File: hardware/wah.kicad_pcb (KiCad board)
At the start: 4 copper layers, 99.1 x 54.5 mm, 32 parts, among them J1 Barrel_Jack_Switch, J2 In, J3 Out, SW1 SW_Push_3PDT, U1 TL072, U2 L78L05_TO92

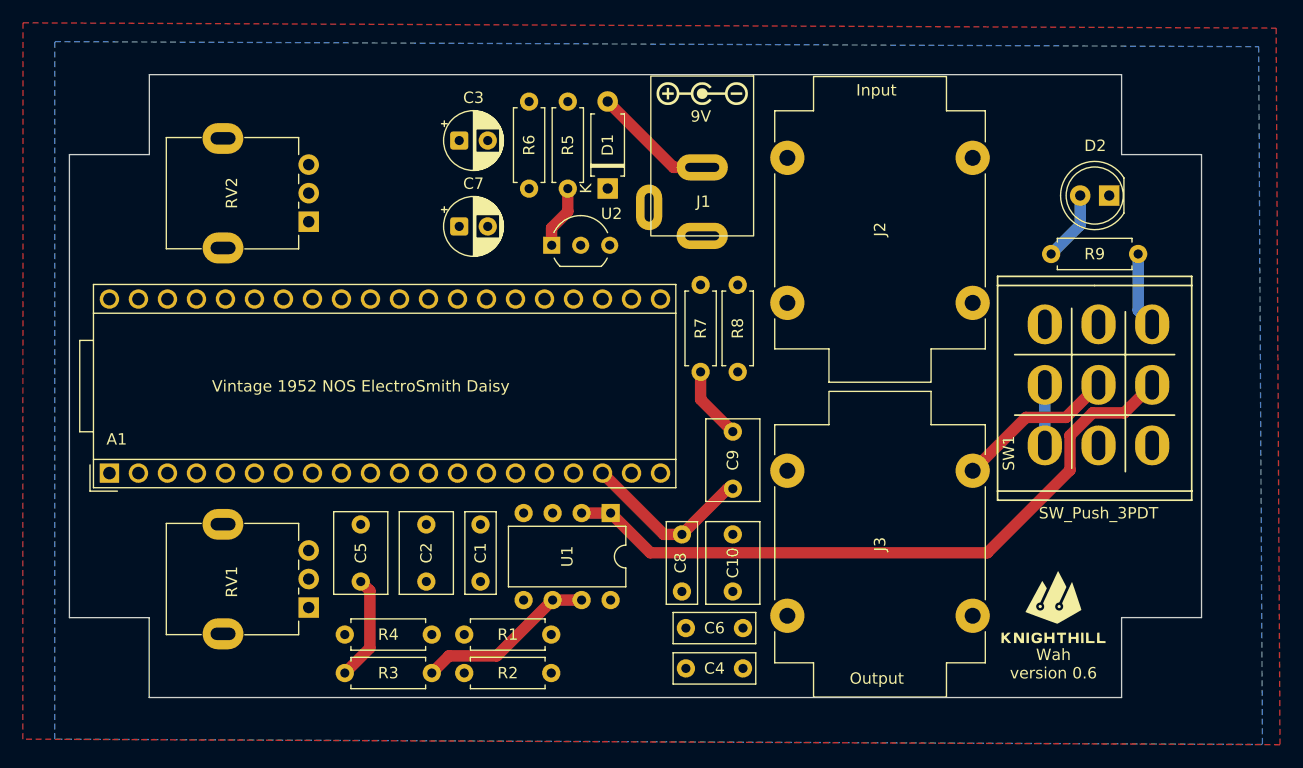
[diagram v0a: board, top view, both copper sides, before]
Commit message: move opamp under daisy
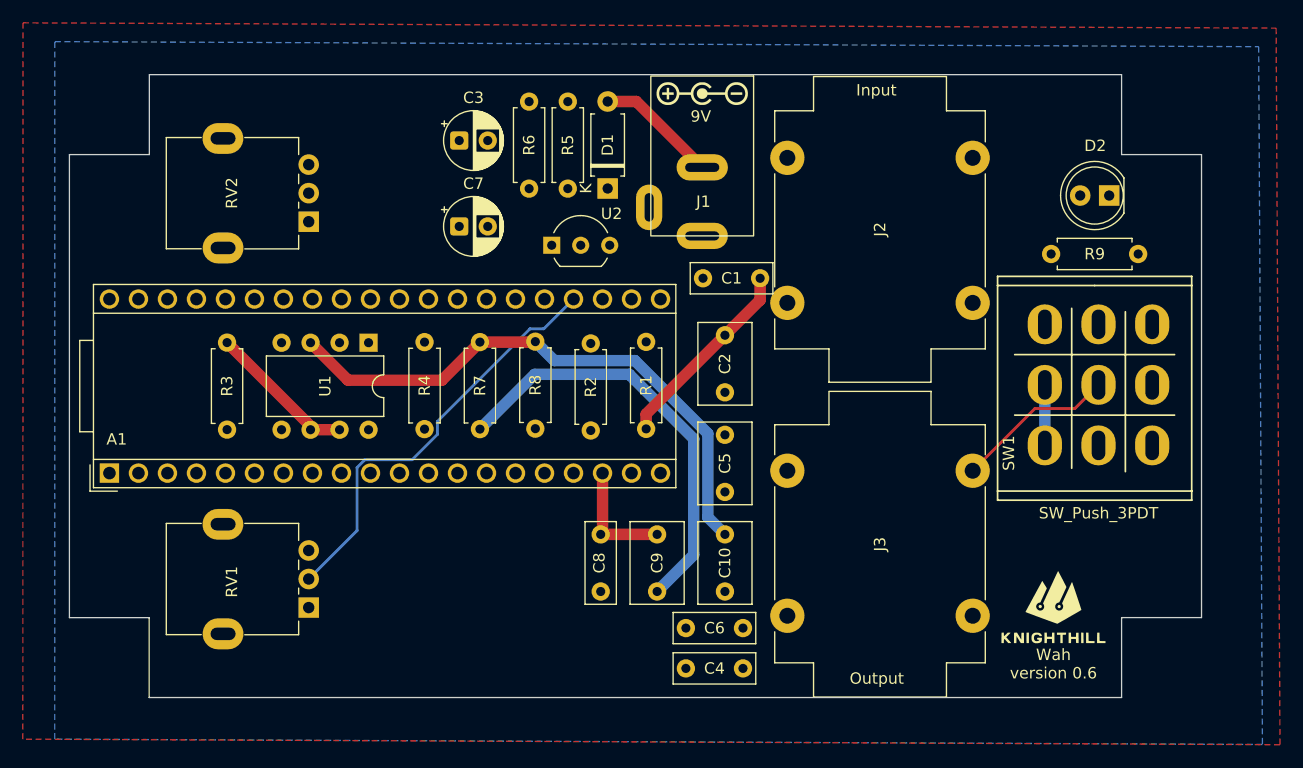
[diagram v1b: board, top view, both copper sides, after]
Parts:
- moved C1 36.1 mm to (102.9, 51.0), turned to 180 degrees
- moved R3 34.0 mm to (56.2, 56.6), turned to -90 degrees
- moved C5 32.8 mm to (99.8, 69.7)
- moved C2 31.0 mm to (99.8, 56.0)
- moved R2 29.1 mm to (88.1, 56.7), turned to -90 degrees
- moved R1 26.9 mm to (92.9, 56.6), turned to -90 degrees
- moved U1 25.9 mm to (68.6, 56.7)
- moved R8 21.7 mm to (83.2, 64.2), turned to 90 degrees
- moved R7 20.0 mm to (78.4, 64.2)
- moved R4 19.3 mm to (73.5, 64.2), turned to 90 degrees
- moved C9 7.74 mm to (93.9, 73.4), turned to -90 degrees
- moved C8 7.11 mm to (88.9, 73.4)
- moved C10 0.69 mm to (99.8, 73.4)
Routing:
- net Net-(C5-Pad1): track 9.25 -> 54.3 mm
- net Net-(U1C-V+): track 58.9 -> 91.2 mm
- net Net-(C9-Pad2): track 6.40 -> 37.7 mm
- net Net-(U1B-+): track 17.7 -> 41.4 mm
- net /FX_OUT: track 59.3 -> 79.9 mm
- net /FX_IN: track 60.3 -> 48.1 mm
- net Net-(U1A-+): track 42.1 -> 50.3 mm
- net Net-(C1-Pad1): track 12.2 -> 17.3 mm
- net /AUDIO_OUT: track 15.3 -> 10.4 mm
- net Net-(U1B--): track 15.8 -> 13.2 mm
- net /POT1: track 36.7 -> 37.3 mm
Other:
- board text removed: "Vintage 1952 NOS ElectroSmith Daisy"
